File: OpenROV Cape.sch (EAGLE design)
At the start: 26 parts, among them T1 2N2222, T2 TIP122

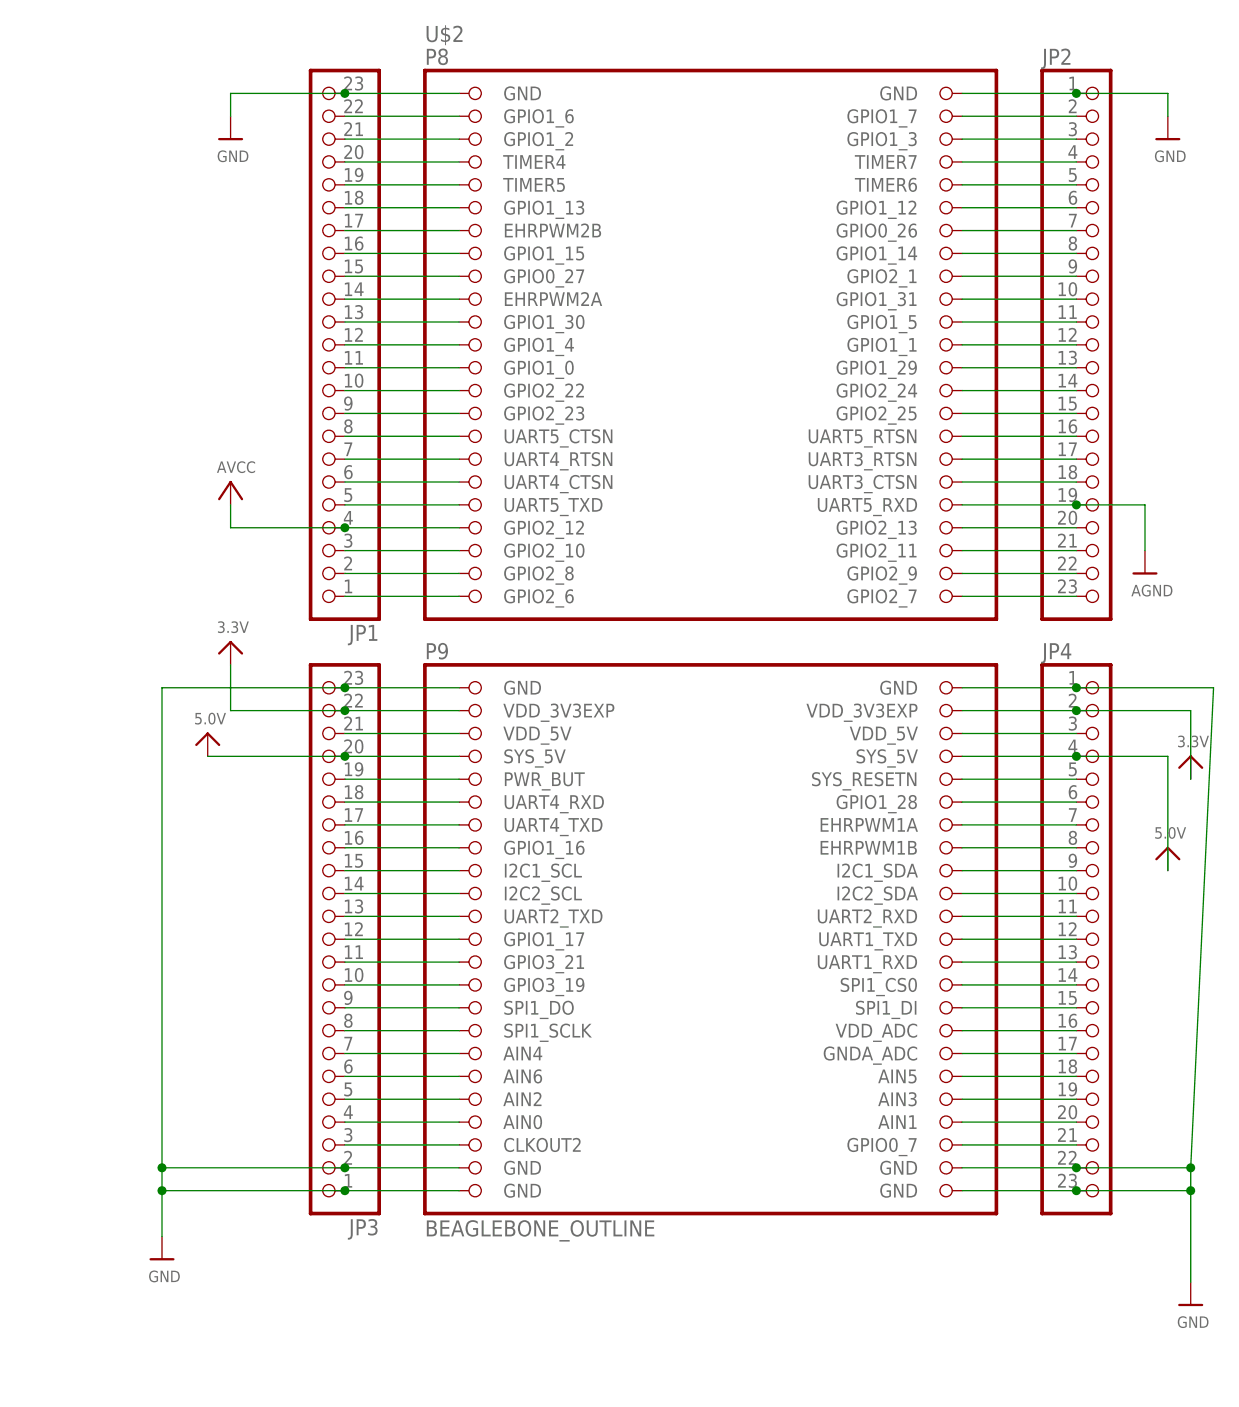
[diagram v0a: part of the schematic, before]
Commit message: removed the extra beagle board header pins to make more room for arduino pins
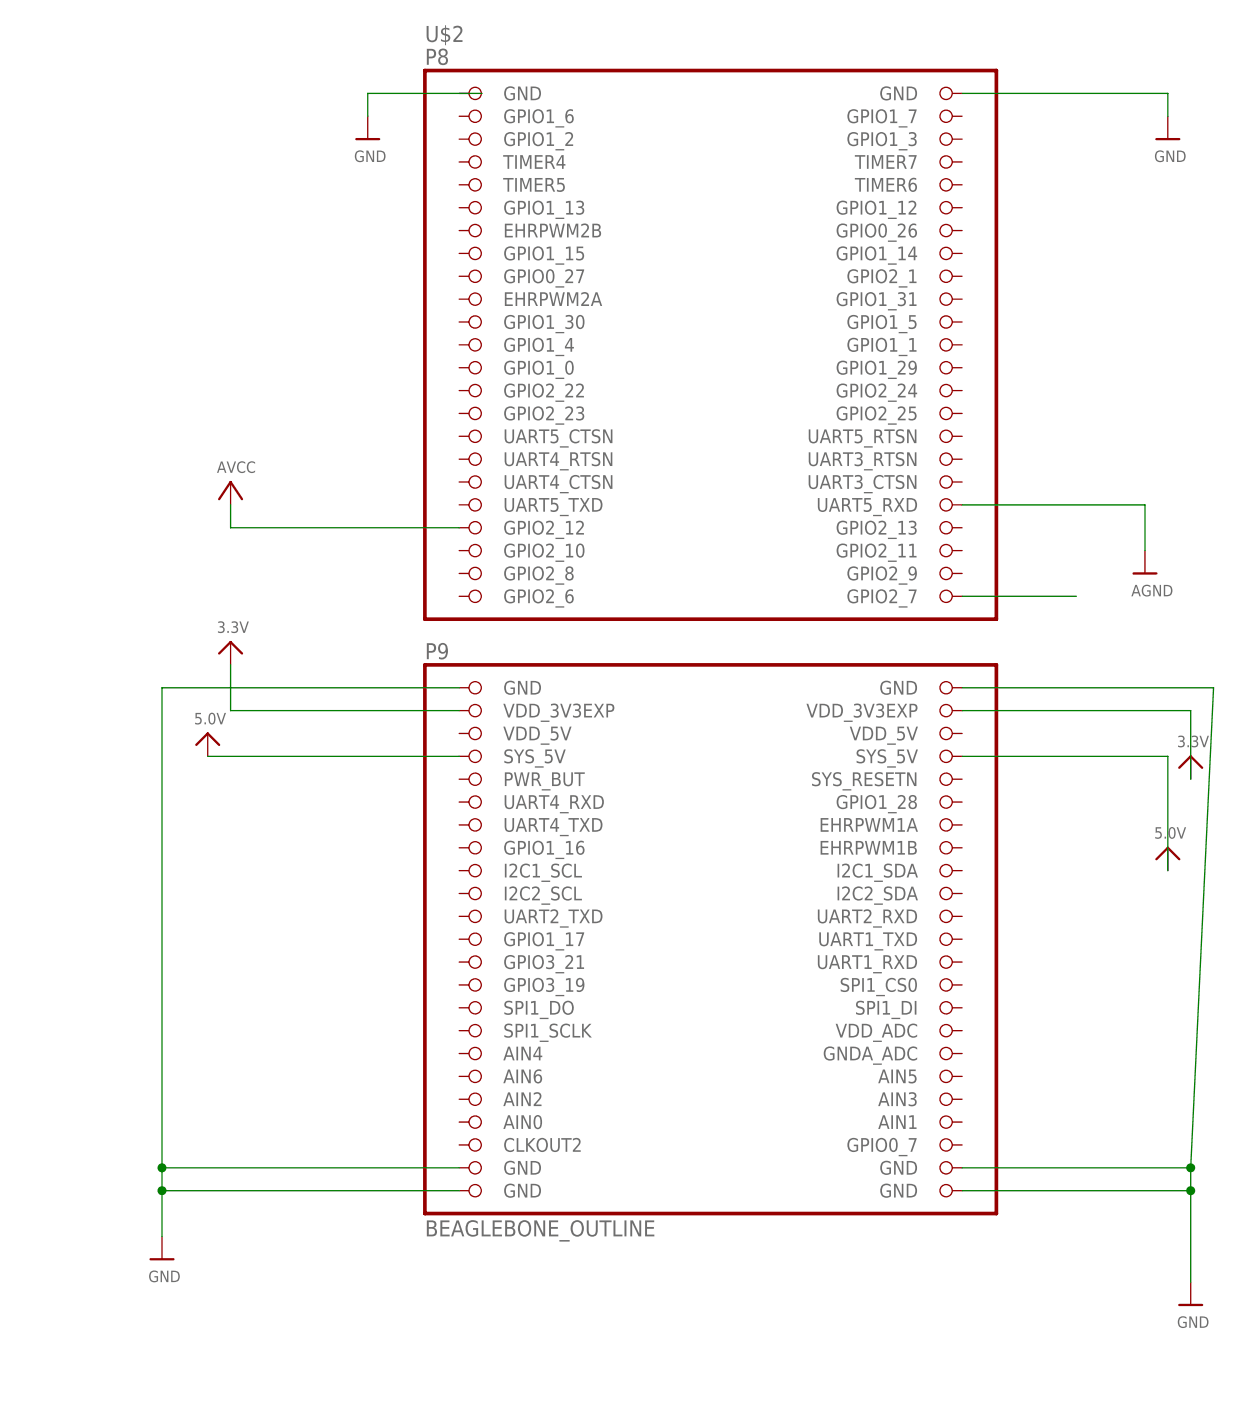
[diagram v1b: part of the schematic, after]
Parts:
- removed JP1, JP2, JP3, JP4: (no value), microbuilder:HEADER-1X23
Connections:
- removed net N$10: JP1.14, U$2.EHRPWM2A
- removed net N$11: JP1.13, U$2.GPIO1_30
- removed net N$12: JP1.12, U$2.GPIO1_4
- removed net N$13: JP1.11, U$2.GPIO1_0
- removed net N$14: JP1.10, U$2.GPIO2_22
- removed net N$15: JP1.9, U$2.GPIO2_23
- removed net N$16: JP1.8, U$2.UART5_CTSN
- removed net N$17: JP1.7, U$2.UART4_RTSN
- removed net N$18: JP1.6, U$2.UART4_CTSN
- removed net N$19: JP1.5, U$2.UART5_TXD
- removed net N$21: JP1.3, U$2.GPIO2_10
- removed net N$22: JP1.2, U$2.GPIO2_8
- removed net N$23: JP1.1, U$2.GPIO2_6
- removed net N$27: JP2.4, U$2.TIMER7
- removed net N$28: JP2.5, U$2.TIMER6
- removed net N$29: JP2.6, U$2.GPIO1_12
- removed net N$30: JP2.7, U$2.GPIO0_26
- removed net N$31: JP2.8, U$2.GPIO1_14
- removed net N$32: JP2.9, U$2.GPIO2_1
- removed net N$33: JP2.10, U$2.GPIO1_31
- removed net N$34: JP2.11, U$2.GPIO1_5
- removed net N$35: JP2.12, U$2.GPIO1_1
- removed net N$36: JP2.13, U$2.GPIO1_29
- removed net N$37: JP2.14, U$2.GPIO2_24
- removed net N$38: JP2.15, U$2.GPIO2_25
- removed net N$39: JP2.16, U$2.UART5_RTSN
- removed net N$4: JP1.20, U$2.TIMER4
- removed net N$40: JP2.17, U$2.UART3_RTSN
- removed net N$41: JP2.18, U$2.UART3_CTSN
- removed net N$43: JP2.20, U$2.GPIO2_13
- removed net N$44: JP2.21, U$2.GPIO2_11
- removed net N$45: JP2.22, U$2.GPIO2_9
- removed net N$47: JP1.22, U$2.GPIO1_6
- removed net N$48: JP1.21, U$2.GPIO1_2
- removed net N$49: JP3.21, U$2.VDD_5V@1
- removed net N$5: JP1.19, U$2.TIMER5
- removed net N$50: JP2.2, U$2.GPIO1_7
- removed net N$51: JP3.19, U$2.PWR_BUT
- removed net N$52: JP3.18, U$2.UART4_RXD
- removed net N$53: JP3.17, U$2.UART4_TXD
- removed net N$54: JP3.16, U$2.GPIO1_16
- removed net N$55: JP3.15, U$2.I2C1_SCL
- removed net N$56: JP3.14, U$2.I2C2_SCL
- removed net N$57: JP3.13, U$2.UART2_TXD
- removed net N$58: JP3.12, U$2.GPIO1_17
- removed net N$59: JP3.11, U$2.GPIO3_21
- removed net N$6: JP1.18, U$2.GPIO1_13
- removed net N$60: JP3.10, U$2.GPIO3_19
- removed net N$61: JP3.9, U$2.SPI1_DO
- removed net N$62: JP3.8, U$2.SPI1_SCLK
- removed net N$63: JP3.7, U$2.AIN4
- removed net N$64: JP3.6, U$2.AIN6
- removed net N$65: JP3.5, U$2.AIN2
- removed net N$66: JP3.4, U$2.AIN0
- removed net N$67: JP3.3, U$2.CLKOUT2
- removed net N$68: JP2.3, U$2.GPIO1_3
- removed net N$69: JP4.21, U$2.GPIO0_7
- removed net N$7: JP1.17, U$2.EHRPWM2B
- removed net N$72: JP4.3, U$2.VDD_5V@2
- removed net N$74: JP4.5, U$2.SYS_RESETN
- removed net N$75: JP4.6, U$2.GPIO1_28
- removed net N$76: JP4.7, U$2.EHRPWM1A
- removed net N$77: JP4.8, U$2.EHRPWM1B
- removed net N$78: JP4.9, U$2.I2C1_SDA
- removed net N$79: JP4.10, U$2.I2C2_SDA
- removed net N$8: JP1.16, U$2.GPIO1_15
- removed net N$80: JP4.11, U$2.UART2_RXD
- removed net N$81: JP4.12, U$2.UART1_TXD
- removed net N$82: JP4.13, U$2.UART1_RXD
- removed net N$83: JP4.14, U$2.SPI1_CS0
- removed net N$84: JP4.15, U$2.SPI1_DI
- removed net N$85: JP4.16, U$2.VDD_ADC
- removed net N$86: JP4.17, U$2.GNDA_ADC
- removed net N$87: JP4.18, U$2.AIN5
- removed net N$88: JP4.19, U$2.AIN3
- removed net N$89: JP4.20, U$2.AIN1
- removed net N$9: JP1.15, U$2.GPIO0_27
- net 3.3V: no longer JP3.22, JP4.2
- net 5.0V: no longer JP3.20, JP4.4
- net AGND: no longer JP2.19
- net AVCC: no longer JP1.4
- net GND: no longer JP1.23, JP2.1, JP3.1, JP3.2, JP3.23, JP4.1, JP4.22, JP4.23, U$2.GND@7
- net N$46: no longer JP2.23

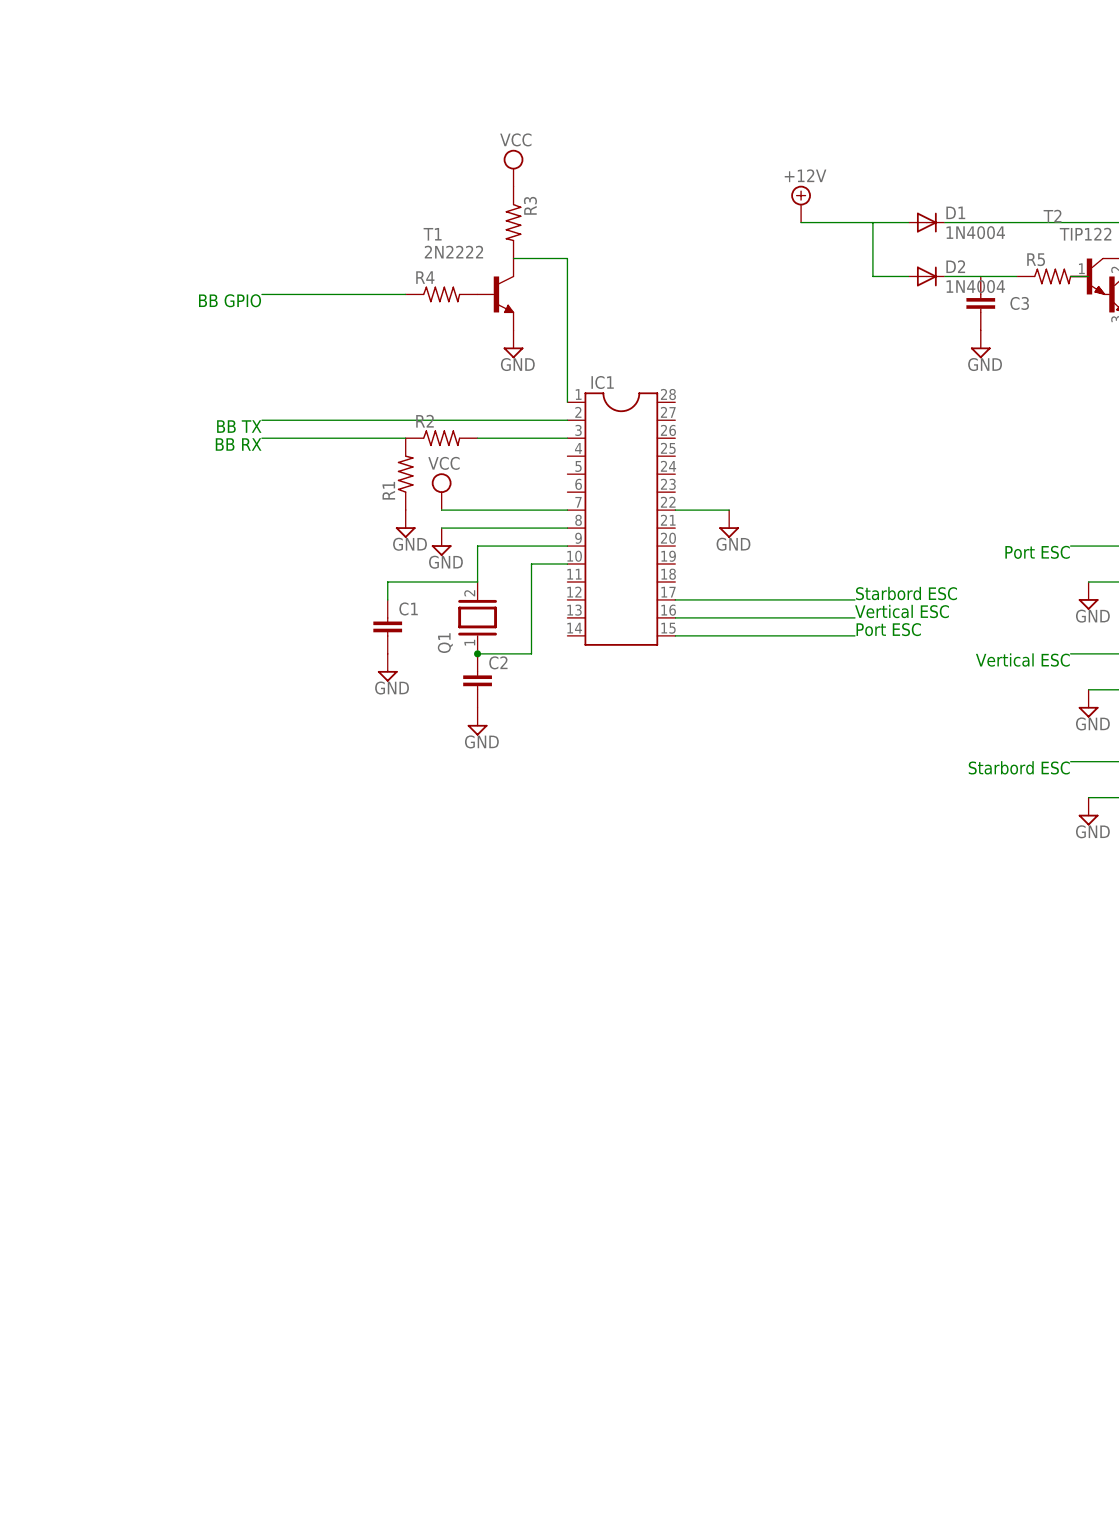
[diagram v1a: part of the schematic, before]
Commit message: swapped out IC1 for official sparkfun atmega328 footprint
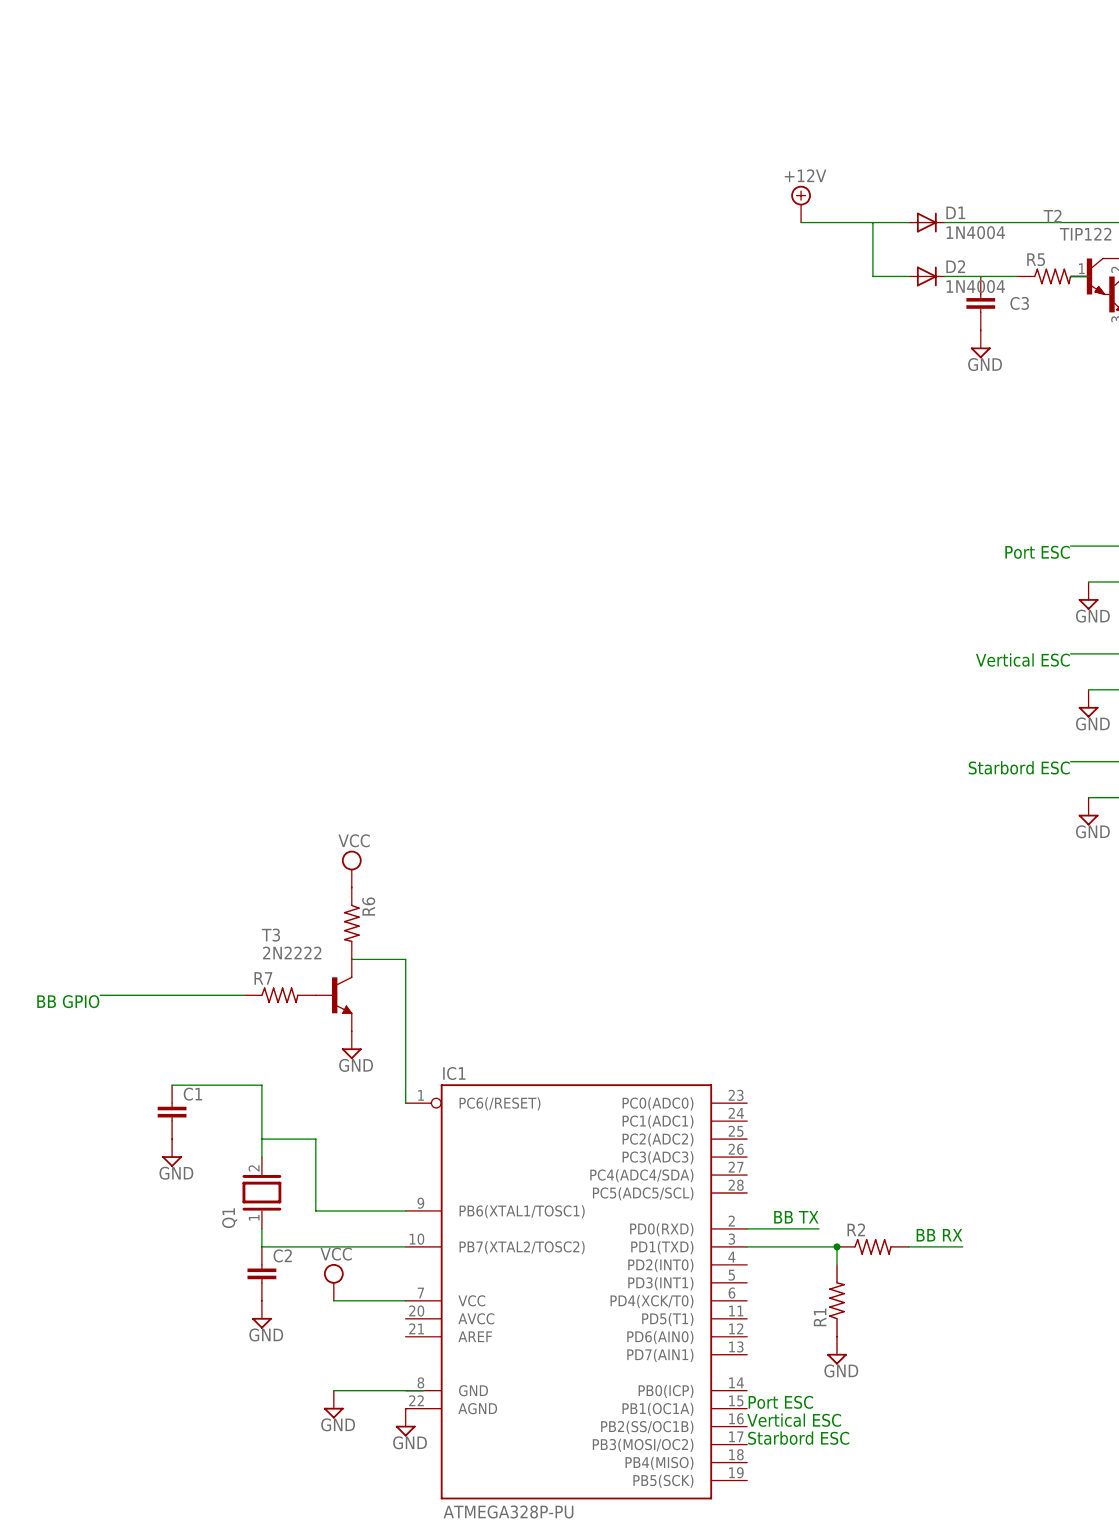
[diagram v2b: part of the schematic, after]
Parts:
- removed R3, R4: (no value), rcl:R-US_0204/7
- removed T1: 2N2222, transistor:2N2222
- added R6, R7: (no value), rcl:R-US_0204/7
- added T3: 2N2222, transistor:2N2222
- IC1: value (none) -> ATMEGA328P-PU; device ic-package:DIL28-4 -> SparkFun:AVR-MEGA8-PPTH
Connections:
- removed net N$20: R4.1
- removed net N$26: IC1.15
- removed net N$3: R4.2, T1.B
- removed net N$42: IC1.16
- removed net N$70: IC1.17
- removed net N$96: IC1.3, R2.2
- new net N$4: IC1.PC6(/RESET), R6.2, T3.C
- new net N$5: R7.2, T3.B
- new net N$6: R7.1
- net GND: now also T3.E; no longer IC1.22, IC1.8, T1.E
- net N$1: now also IC1.PD0(RXD); no longer IC1.2
- net N$2: now also R2.2; no longer IC1.1, R3.2, T1.C
- net N$24: now also IC1.PB7(XTAL2/TOSC2); no longer IC1.10
- net N$25: now also IC1.PB6(XTAL1/TOSC1); no longer IC1.9
- net VCC: now also IC1.VCC@1, R6.1; no longer IC1.7, R3.1
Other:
- moved on the sheet: C1, C2, Q1, R1, R2
